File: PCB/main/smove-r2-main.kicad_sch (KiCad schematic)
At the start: 36 parts, among them J1 TYPE-C-31-M-12, J2 PH2 protected pack, J3 UART 3V3 / DNF, J4 PH4 to carrier, SW2 RESET, SW3 BOOT / USER, U1 ESP32-C3-MINI-1-N4, U4 AP2112K-3.3TRG1, U6 BQ24074RGTR, U8 USBLC6-2SC6, U9 PESD5V0S2BT,215

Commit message: Split main schematic into wired USB Power Compute sheets and document IMU housing alignment
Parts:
- removed C1: 4.7uF / 16V, smove-r2-main:C_0603_1608Metric, symbol Device:C
- removed C10: 1uF / 25V, smove-r2-main:C_0402_1005Metric, symbol Device:C
- removed C11, C4: 100nF / 16V, smove-r2-main:C_0402_1005Metric, symbol Device:C
- removed C13, C2: 47uF / 6.3V, smove-r2-main:C_0805_2012Metric, symbol Device:C
- removed C3: 22uF / 10V, smove-r2-main:C_0805_2012Metric, symbol Device:C
- removed D1: LTST-C19HE1WT / CA, smove-r2-main:LED_LiteOn_LTST-C19HE1WT, symbol smove-r2-main:D1
- removed J1: TYPE-C-31-M-12, smove-r2-main:USB_C_Receptacle_HRO_TYPE-C-31-M-12, symbol smove-r2-main:J1
- removed J2: PH2 protected pack, smove-r2-main:JST_PH_S2B-PH-SM4-TB_1x02-1MP_P2.00mm_Horizontal, symbol smove-r2-main:J2
- removed J3: UART 3V3 / DNF, smove-r2-main:Debug_5, symbol smove-r2-main:J3
- removed J4: PH4 to carrier, smove-r2-main:JST_PH_S4B-PH-SM4-TB_1x04-1MP_P2.00mm_Horizontal, symbol smove-r2-main:J4
- removed R1, R2: 5.1k, smove-r2-main:R_0402_1005Metric, symbol Device:R
- removed R10, R23, R7, R8, R9: 10k, smove-r2-main:R_0402_1005Metric, symbol Device:R
- removed R11, R12, R13: 1k, smove-r2-main:R_0402_1005Metric, symbol Device:R
- removed R14, R15, R5: 100k, smove-r2-main:R_0402_1005Metric, symbol Device:R
- removed R21: 8.2k, smove-r2-main:R_0402_1005Metric, symbol Device:R
- removed R22: 4.7k, smove-r2-main:R_0402_1005Metric, symbol Device:R
- removed R3, R4: 22R, smove-r2-main:R_0402_1005Metric, symbol Device:R
- removed SW2: RESET, smove-r2-main:TS1088, symbol Switch:SW_Push
- removed SW3: BOOT / USER, smove-r2-main:TS1088, symbol Switch:SW_Push
- removed U1: ESP32-C3-MINI-1-N4, smove-r2-main:ESP32-C3-MINI-1, symbol smove-r2-main:U1
- removed U4: AP2112K-3.3TRG1, smove-r2-main:SOT-23-5, symbol smove-r2-main:U4
- removed U6: BQ24074RGTR, smove-r2-main:BQ24074_RGT, symbol smove-r2-main:U6
- removed U8: USBLC6-2SC6, smove-r2-main:SOT-23-6, symbol smove-r2-main:U8
- removed U9: PESD5V0S2BT,215, smove-r2-main:SOT-23, symbol smove-r2-main:U9
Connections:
- no-connect marks 21 -> 0
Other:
- added sheet Compute (compute.kicad_sch)
- added sheet Power (power.kicad_sch)
- added sheet USB (usb.kicad_sch)
- note added: "Crossings without junction dots are NOT connected. Placement and routing unchanged."
- note added: "ESP32-C3 / reset / boot / RGB J4 -> separate IMU carrier PCB PH4: 1=3V3, 2=GND 3=SDA, 4=SCL; <=50mm Carrier U2: direct on its root No nested IMU sheets"
- note added: "One main PCB, three functional pages. Green lines are electrical hierarchical connections."
- note added: "Protected pack J2 U6 charger -> U4 LDO"
- note added: "Prototype only. Supervised off-body charging; no TS cell-temperature sensing."
- note added: "USB data / ESD"
- note added: "sMove R2 | WIRED SYSTEM FLOW"
- note removed: "Charge ONLY supervised, off-body, qualified protected pack and independent bench temperature monitoring. Cell acceptance >=121mA and 4.23V."
- note removed: "NO cell sensing: TS 10k bias permitted by TI. Default timers: TMR open. ITERM open. CE/EN1/EN2 grounded."
- note removed: "Native USB: disconnect before host sleep/off. ROM/crash does not enforce data isolation."
- note removed: "PGOOD_N low = valid USB. Firmware detach on loss. ADC is an LDO headroom screen, NOT a fuel gauge."
- note removed: "PH4: 1=3V3, 2=GND, 3=SDA, 4=SCL <=50mm; carrier owns pulls + 1V8 + translation."
- note removed: "USB100 fixed (90mA guaranteed-min input). Protected 4.2V pack only. No automatic cell-temperature sensing."
- note removed: "sMove R2 MAIN | one-sheet wiring | ENGINEERING PROTOTYPE"
- title: sMove R2 MAIN -> sMove R2 / System flow

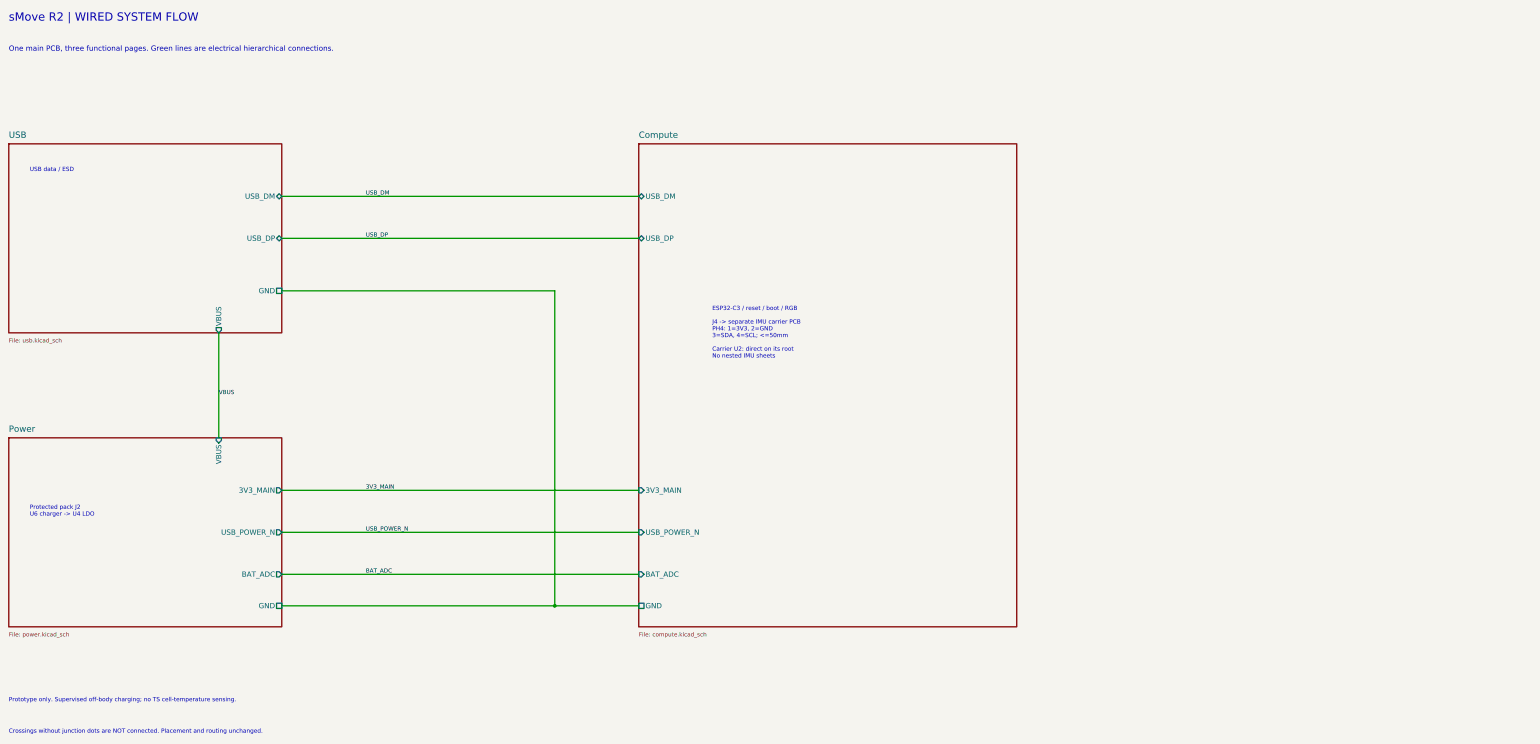
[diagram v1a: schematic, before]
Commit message: Recover compact native delivery from preserved autostash and hash-matched objects
Explicitly commit all 142 recovery paths (51 restored tracked modifications, 91 additions including recovered assets and forensic verification evidence). Preserve the original 30 merged paths unchanged. Do not apply the historical unused-footprint deletion.

Restore exact compact PCB/schematics/FCStd/source/export bytes; all 138 delivery-manifest entries match. Fresh electrical 1214/1214, source/export coherence 657/657, mechanical 2087/2088 with original conservative PH2 reservation gate retained; 7 groups and 58 individual links independently movable.

Original 152-path staging index is unavailable: preserve all 1004 initially unreachable objects, record pathname confidence, and do not claim proven recovery of every original pathname. GUI casing launch remains blocked by desktop lock screen. No merge, redesign, deletion or advisor activity.
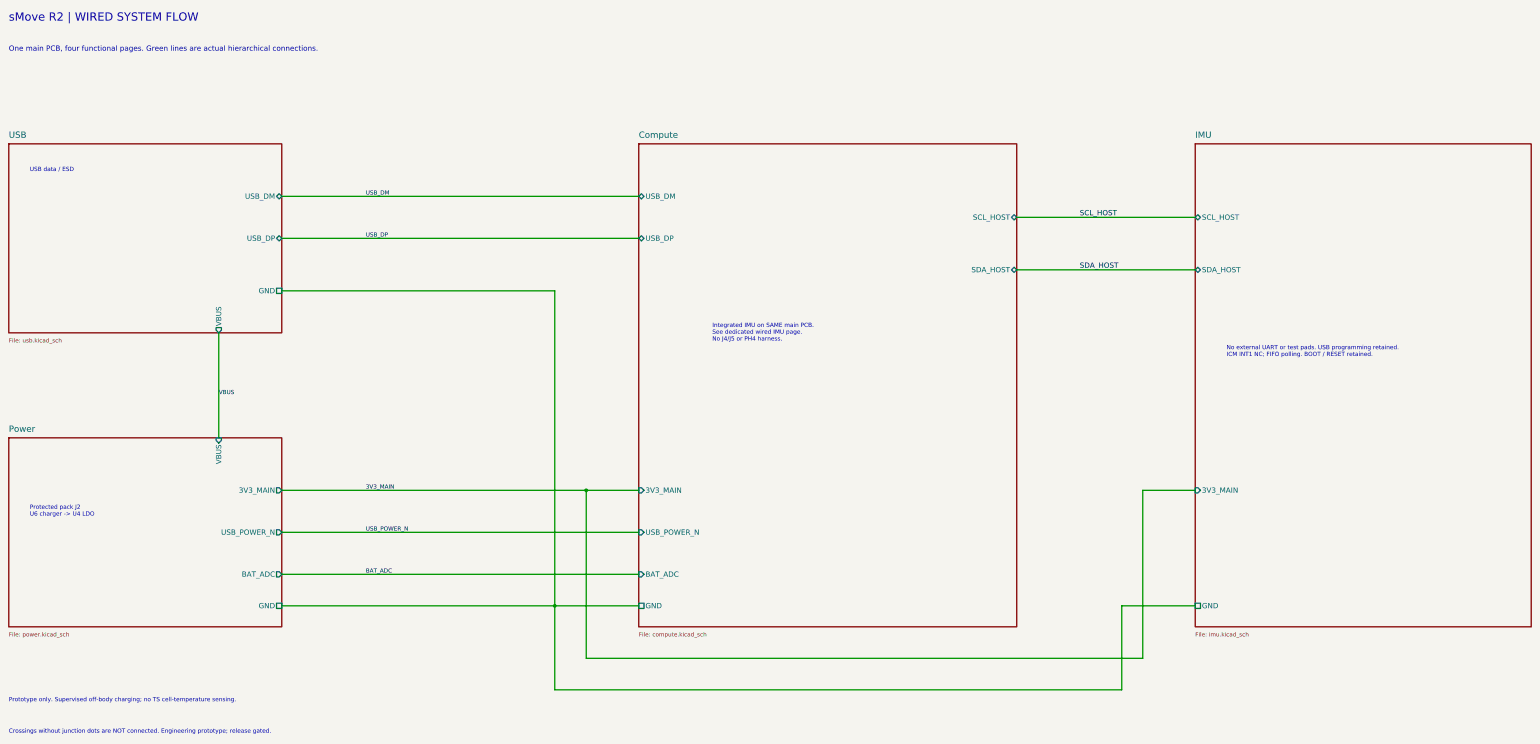
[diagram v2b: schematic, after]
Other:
- added sheet IMU (imu.kicad_sch)
- sheet Compute ports: added SCL_HOST, SDA_HOST; removed none
- note added: "Crossings without junction dots are NOT connected. Engineering prototype; release gated."
- note added: "Integrated IMU on SAME main PCB. See dedicated wired IMU page. No J4/J5 or PH4 harness."
- note added: "No external UART or test pads. USB programming retained. ICM INT1 NC; FIFO polling. BOOT / RESET retained."
- note added: "One main PCB, four functional pages. Green lines are actual hierarchical connections."
- note removed: "Crossings without junction dots are NOT connected. Placement and routing unchanged."
- note removed: "ESP32-C3 / reset / boot / RGB J4 -> separate IMU carrier PCB PH4: 1=3V3, 2=GND 3=SDA, 4=SCL; <=50mm Carrier U2: direct on its root No nested IMU sheets"
- note removed: "One main PCB, three functional pages. Green lines are electrical hierarchical connections."
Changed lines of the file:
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@@
   (version 20250114)
   (generator "eeschema")
-  (paper "A4")
+  (paper "A3")
   (title_block
     (title "sMove R2 / System flow")
     (rev "R2 ENG")
-    (comment 1 "MAIN PCB - THREE FUNCTIONAL CHILD PAGES"))
+    (comment 1 "MAIN PCB - USB / POWER / COMPUTE / INTEGRATED IMU"))
   (sheet
     (at 25.4 45.72)
@@
           (size 1.27 1.27))
         (justify left))
+)
+    (pin "SCL_HOST" bidirectional
+      (at 269.24 63.5 0)
+      (effects
+        (font
+          (size 1.27 1.27))
+        (justify right))
+)
+    (pin "SDA_HOST" bidirectional
+      (at 269.24 76.2 0)
+      (effects
+        (font
+          (size 1.27 1.27))
+        (justify right))
 ))
   (wire
@@
       (xy 91.44 68.58)
       (xy 177.8 68.58))
-    (stroke
-      (width 0)
-      (type default))
-)
-  (wire
-    (pts
-      (xy 91.44 129.54)
-      (xy 177.8 129.54))
     (stroke
       (width 0)
@@
       (justify left))
 )
-  (text "One main PCB, three functional pages. Green lines are electrical hierarchical connections."
+  (text "One main PCB, four functional pages. Green lines are actual hierarchical connections."
     (at 25.4 22.86 0)
     (effects
@@
       (justify left))
 )
-  (text "ESP32-C3 / reset / boot / RGB\n\nJ4 -> separate IMU carrier PCB\nPH4: 1=3V3, 2=GND\n3=SDA, 4=SCL; <=50mm\n\nCarrier U2: direct on its root\nNo nested IMU sheets"
+  (text "Integrated IMU on SAME main PCB.\nSee dedicated wired IMU page.\nNo J4/J5 or PH4 harness."
     (at 195.58 91.44 0)
     (effects
@@
       (justify left))
 )
-  (text "Crossings without junction dots are NOT connected. Placement and routing unchanged."
+  (text "Crossings without junction dots are NOT connected. Engineering prototype; release gated."
     (at 25.4 187.96 0)
     (effects
@@
   (sheet_instances
     (path "/"
-      (page "1"))))
+      (page "1")))
+  (wire
+    (pts
+      (xy 269.24 63.5)
+      (xy 312.42 63.5))
+    (stroke
+      (width 0)
+      (type default))
+)
+  (wire
+    (pts
+      (xy 269.24 76.2)
+      (xy 312.42 76.2))
+    (stroke
+      (width 0)
+      (type default))
+)
+  (sheet
+    (at 312.42 45.72)
+    (size 81.28 116.84)
+    (stroke
+      (width .254)
+      (type default))
+    (fill
+      (color 0 0 0 0))
+    (property "Sheetname" "IMU"
+      (at 312.42 44.45 0)
+      (effects
+        (font
+          (size 1.52 1.52))
+        (justify left bottom)))
+    (property "Sheetfile" "imu.kicad_sch"
+      (at 312.42 163.83 0)
+      (effects
+        (font
+          (size 1 1))
+        (justify left top)))
+    (instances
+      (project "smove-r2-main"
+        (path "/8e261347-838a-5848-981d-f693675e8aa0"
+          (page "5"))))
+    (pin "SCL_HOST" bidirectional
+      (at 312.42 63.5 180)
+      (effects
+        (font
+          (size 1.27 1.27))
+        (justify left))
+)
+    (pin "SDA_HOST" bidirectional
+      (at 312.42 76.2 180)
+      (effects
+        (font
+          (size 1.27 1.27))
+        (justify left))
+)
+    (pin "3V3_MAIN" input
+      (at 312.42 129.54 180)
+      (effects
+        (font
+          (size 1.27 1.27))
+        (justify left))
+)
+    (pin "GND" passive
+      (at 312.42 157.48 180)
+      (effects
+        (font
+          (size 1.27 1.27))
+        (justify left))
+))
+  (text "No external UART or test pads. USB programming retained.\nICM INT1 NC; FIFO polling. BOOT / RESET retained."
+    (at 320 96 0)
+    (effects
+      (font
+        (size 1.02 1.02))
+      (justify left))
+)
+  (wire
+    (pts
+      (xy 165.1 129.54)
+      (xy 165.1 170.18))
+    (stroke
+      (width 0)
+      (type default))
+)
+  (wire
+    (pts
+      (xy 165.1 170.18)
+      (xy 299.72 170.18))
+    (stroke
+      (width 0)
+      (type default))
+)
+  (wire
+    (pts
+      (xy 299.72 170.18)
+      (xy 299.72 129.54))
+    (stroke
+      (width 0)
+      (type default))
+)
+  (wire
+    (pts
+      (xy 299.72 129.54)
+      (xy 312.42 129.54))
+    (stroke
+      (width 0)
+      (type default))
+)
+  (wire
+    (pts
+      (xy 157.48 157.48)
+      (xy 157.48 177.8))
+    (stroke
+      (width 0)
+      (type default))
+)
+  (wire
+    (pts
+      (xy 157.48 177.8)
+      (xy 294.64 177.8))
+    (stroke
+      (width 0)
+      (type default))
+)
+  (wire
+    (pts
+      (xy 294.64 177.8)
+      (xy 294.64 157.48))
+    (stroke
+      (width 0)
+      (type default))
+)
+  (wire
+    (pts
+      (xy 294.64 157.48)
+      (xy 312.42 157.48))
+    (stroke
+      (width 0)
+      (type default))
+)
+  (wire
+    (pts
+      (xy 91.44 129.54)
+      (xy 165.1 129.54))
+    (stroke
+      (width 0)
+      (type default))
+)
+  (wire
+    (pts
+      (xy 165.1 129.54)
+      (xy 177.8 129.54))
+    (stroke
+      (width 0)
+      (type default))
+)
+  (junction
+    (at 165.1 129.54)
+    (diameter 0)
+    (color 0 0 0 0)
+)
+  (label "SCL_HOST"
+    (at 284.48 63.5 0)
+    (effects
+      (font
+        (size 1.27 1.27))
+      (justify left bottom))
+)
+  (label "SDA_HOST"
+    (at 284.48 76.2 0)
+    (effects
+      (font
+        (size 1.27 1.27))
+      (justify left bottom))
+))

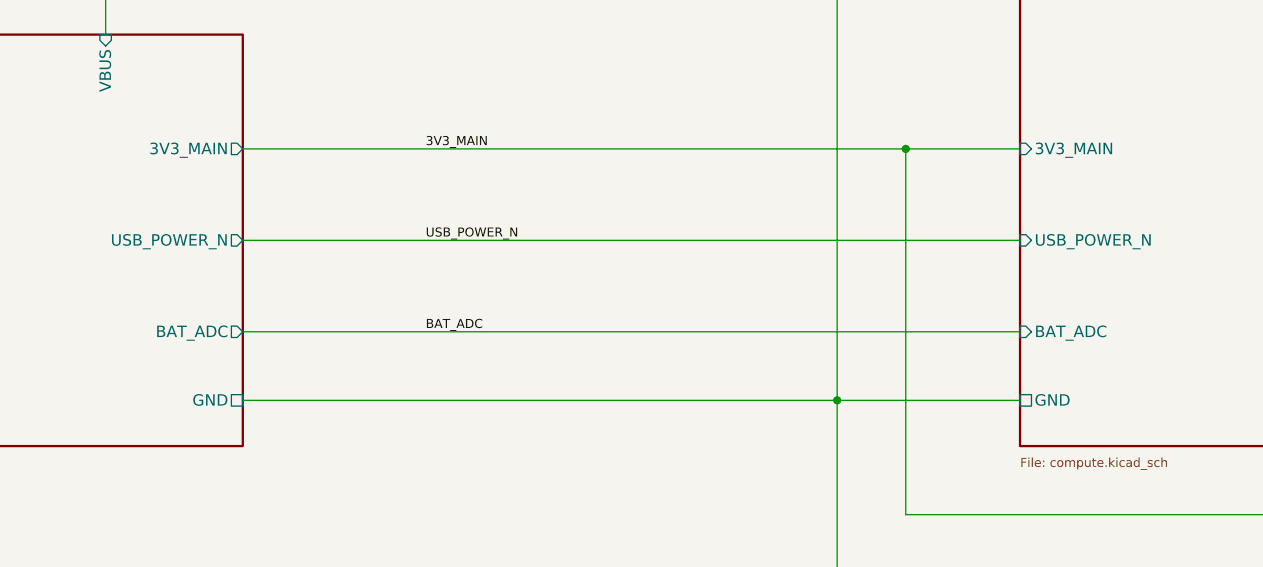
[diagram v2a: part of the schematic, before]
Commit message: Add Battery on/off switch
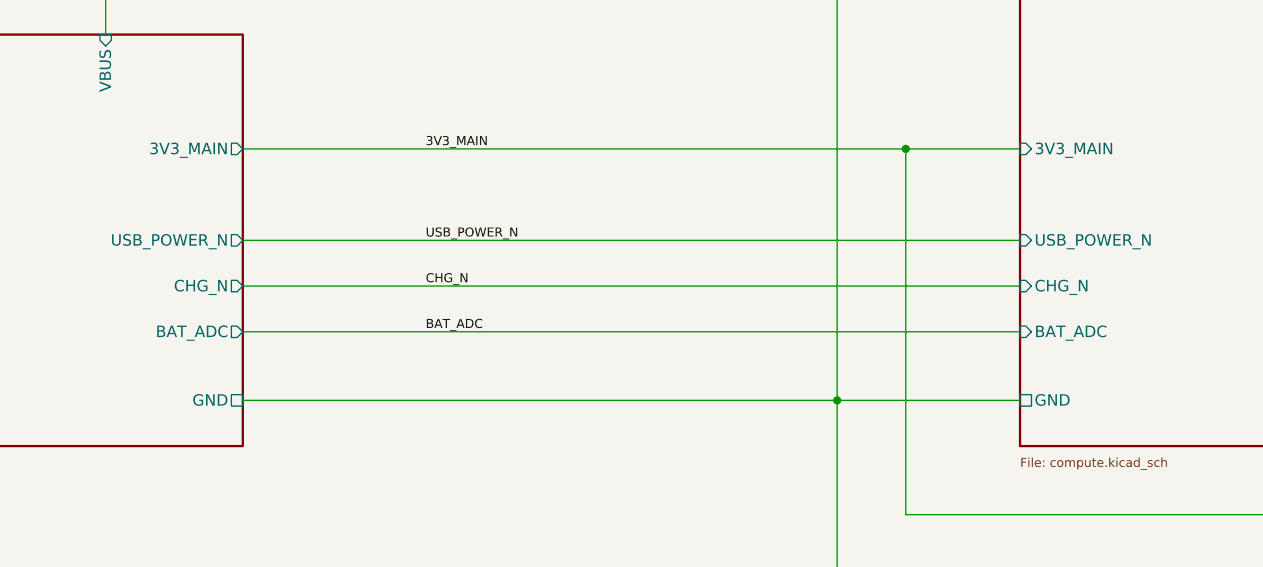
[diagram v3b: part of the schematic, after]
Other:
- sheet Compute ports: added CHG_N; removed none
- sheet Power ports: added CHG_N; removed none
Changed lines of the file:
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@@
+          (size 1.27 1.27))
+        (justify right))
+)
+    (pin "CHG_N" output
+      (at 91.44 144.78 0)
+      (effects
+        (font
           (size 1.27 1.27))
         (justify right))
@@
           (size 1.27 1.27))
         (justify right))
+)
+    (pin "CHG_N" input
+      (at 177.8 144.78 180)
+      (effects
+        (font
+          (size 1.27 1.27))
+        (justify left))
 ))
   (wire
@@
         (size 1.27 1.27))
       (justify left bottom))
+)
+  (wire
+    (pts
+      (xy 91.44 144.78)
+      (xy 177.8 144.78))
+    (stroke
+      (width 0)
+      (type default))
+)
+  (label "CHG_N"
+    (at 111.76 144.78 0)
+    (effects
+      (font
+        (size 1 1))
+      (justify left bottom))
 ))
